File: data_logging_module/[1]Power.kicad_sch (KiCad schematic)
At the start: 14 parts, among them J3 Screw_Terminal_01x02, U2 TLV62569DBV

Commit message: Initial scheme
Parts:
- removed D9: D, Diode_SMD:D_PowerDI-123, symbol Device:D
- removed J3: Screw_Terminal_01x02, esp32s3_watches:terminal_block, symbol Connector:Screw_Terminal_01x02
- added C104, C105: 22u, Capacitor_SMD:C_0805_2012Metric, symbol Device:C
- added R107: 10R, Resistor_SMD:R_0805_2012Metric, symbol Device:R
- added U101: HT7533-1, Package_TO_SOT_SMD:SOT-89-3, symbol Regulator_Linear:HT75xx-1-SOT89
- renumbered C6 to C100, C7 to C101, C8 to C102, C9 to C103, C10 to C106, D10 to D100, L1 to L100, L2 to L101, R7 to R104, R8 to R105, R9 to R106, U2 to U100
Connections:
- net +5V: now also R107.2
- net GND: now also C104.2, C105.2, U101.1 (GND)
- new net +3.3VA: C105.1, U101.3 (VOUT)
- new net +5V_FILT: C104.1, R107.1, U101.2 (VIN)
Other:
- note added: "100mA max."
- note added: "Analog Supplies"
- note added: "C(in/out)>10uF"
- note added: "P(R)>1/8W"
- moved on the sheet: C100, C101, C102, C103, C106, D100, L100, L101, R104, R105, R106, U100

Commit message: BOM updates
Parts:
- C100, C101: Manufacturer Part Number (none) -> CL21B105KBFNNNE
- C102, C103: Manufacturer Part Number (none) -> CL21A226MAYNNNE
- C104, C105: value 22u -> 22uF; Manufacturer Samwha Capacitor -> Samsung Electro-Mechanics; Manufacturer Part Number CS2012X5R226M160NRE -> CL21A226MAYNNNE
- L100: Manufacturer Part Number (none) -> LQG18HN10NJ00D
- L101: footprint esp32s3_watches:MWSA0603S -> data_logging_module:MWSA0603S; Manufacturer Part Number (none) -> FXL0630-150-M
- R104: Manufacturer Part Number (none) -> 0805W8F1003T5E
- R105: Manufacturer Part Number (none) -> 0805W8F2202T5E
- R106: Manufacturer Part Number (none) -> ARG05FTC5000
- U100: Manufacturer Part Number (none) -> TLV62569DBVR
- U101: Manufacturer Part Number HT7533-1 -> HT7533-1
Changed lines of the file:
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@@
 			)
 		)
-		(property "Value" "22u"
+		(property "Value" "22uF"
 			(at 127 118.11 0)
 			(effects
@@
 			)
 		)
-		(property "Manufacturer" "Samwha Capacitor"
+		(property "Manufacturer" "Samsung Electro-Mechanics"
 			(at 123.19 116.84 0)
 			(effects
@@
 			)
 		)
-		(property "Manufacturer Part Number" "CS2012X5R226M160NRE"
+		(property "Manufacturer Part Number" "CL21A226MAYNNNE"
 			(at 123.19 116.84 0)
 			(effects
@@
 			)
 		)
+		(property "Manufacturer Part Number" "LQG18HN10NJ00D"
+			(at 77.47 45.72 0)
+			(effects
+				(font
+					(size 1.27 1.27)
+				)
+				(hide yes)
+			)
+		)
 		(pin "1"
 		)
@@
 			)
 		)
+		(property "Manufacturer Part Number" "CL21B105KBFNNNE"
+			(at 64.77 52.07 0)
+			(effects
+				(font
+					(size 1.27 1.27)
+				)
+				(hide yes)
+			)
+		)
 		(pin "1"
 		)
@@
 			)
 		)
+		(property "Manufacturer Part Number" "ARG05FTC5000"
+			(at 219.71 55.88 0)
+			(effects
+				(font
+					(size 1.27 1.27)
+				)
+				(hide yes)
+			)
+		)
 		(pin "1"
 		)
@@
 			)
 		)
-		(property "Manufacturer Part Number" "HT7533-1 "
+		(property "Manufacturer Part Number" "HT7533-1"
 			(at 106.68 113.03 0)
 			(effects
@@
 			)
 		)
+		(property "Manufacturer Part Number" "TLV62569DBVR"
+			(at 130.81 48.26 0)
+			(effects
+				(font
+					(size 1.27 1.27)
+				)
+				(hide yes)
+			)
+		)
 		(pin "1"
 		)
@@
 			)
 		)
+		(property "Manufacturer Part Number" "CL21A226MAYNNNE"
+			(at 163.83 52.07 0)
+			(effects
+				(font
+					(size 1.27 1.27)
+				)
+				(hide yes)
+			)
+		)
 		(pin "1"
 		)
@@
 		)
 		(property "Manufacturer Product Number" "CL21A226MAYNNNE"
+			(at 105.41 52.07 0)
+			(effects
+				(font
+					(size 1.27 1.27)
+				)
+				(hide yes)
+			)
+		)
+		(property "Manufacturer Part Number" "CL21A226MAYNNNE"
 			(at 105.41 52.07 0)
 			(effects
@@
 			)
 		)
-		(property "Value" "22u"
+		(property "Value" "22uF"
 			(at 93.98 118.11 0)
 			(effects
@@
 			)
 		)
-		(property "Manufacturer" "Samwha Capacitor"
+		(property "Manufacturer" "Samsung Electro-Mechanics"
 			(at 90.17 116.84 0)
 			(effects
@@
 			)
 		)
-		(property "Manufacturer Part Number" "CS2012X5R226M160NRE"
+		(property "Manufacturer Part Number" "CL21A226MAYNNNE"
 			(at 90.17 116.84 0)
 			(effects
@@
 			)
 		)
+		(property "Manufacturer Part Number" "CL21B105KBFNNNE"
+			(at 90.17 52.07 0)
+			(effects
+				(font
+					(size 1.27 1.27)
+				)
+				(hide yes)
+			)
+		)
 		(pin "1"
 		)
@@
 			)
 		)
-		(property "Footprint" "esp32s3_watches:MWSA0603S"
+		(property "Footprint" "data_logging_module:MWSA0603S"
 			(at 152.4 45.72 0)
 			(effects
@@
 		)
 		(property "Manufacturer Product Number" "FXL0630-150-M"
+			(at 152.4 45.72 0)
+			(effects
+				(font
+					(size 1.27 1.27)
+				)
+				(hide yes)
+			)
+		)
+		(property "Manufacturer Part Number" "FXL0630-150-M"
 			(at 152.4 45.72 0)
 			(effects
@@
 			)
 		)
+		(property "Manufacturer Part Number" "0805W8F1003T5E"
+			(at 181.61 52.07 0)
+			(effects
+				(font
+					(size 1.27 1.27)
+				)
+				(hide yes)
+			)
+		)
 		(pin "1"
 		)
@@
 			(at 181.61 66.04 0)
 			(effects
+				(font
+					(size 1.27 1.27)
+				)
+				(hide yes)
+			)
+		)
+		(property "Manufacturer Part Number" "0805W8F2202T5E"
+			(at 181.61 66.04 0)
+			(effects

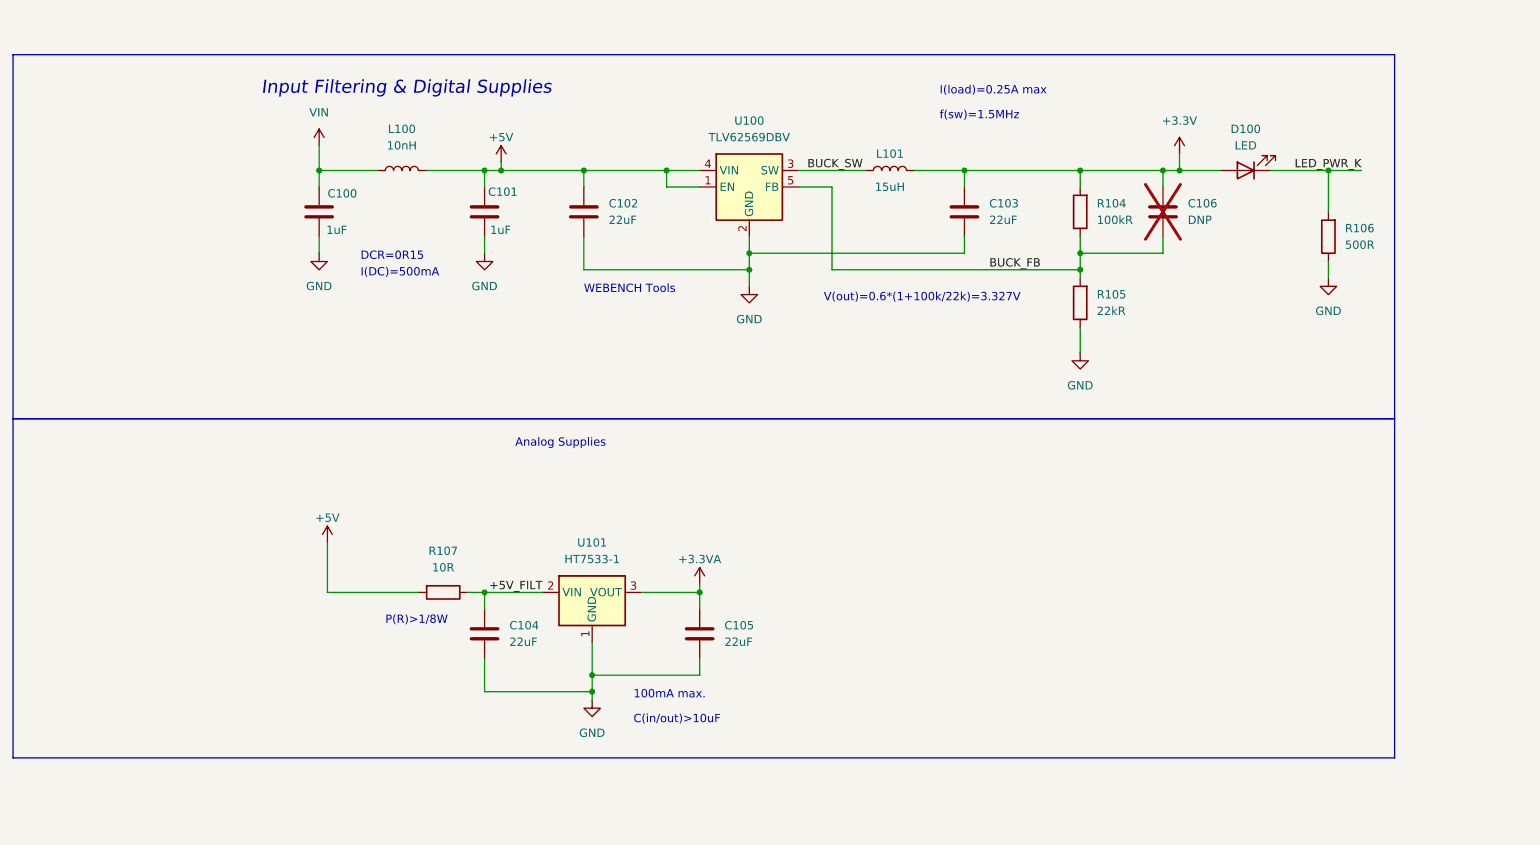
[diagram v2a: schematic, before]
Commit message: PCB initial layout
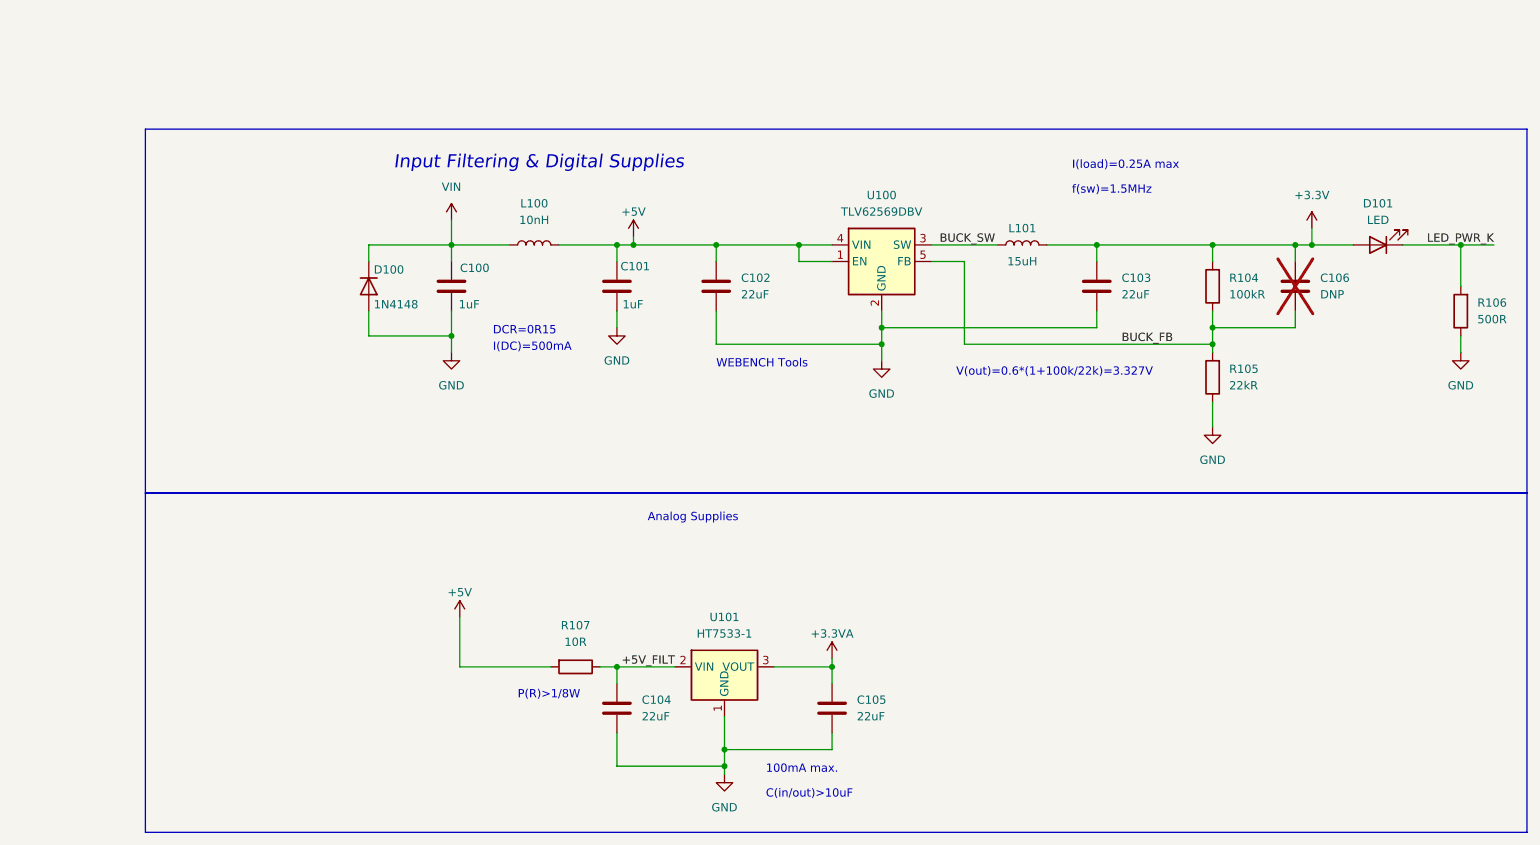
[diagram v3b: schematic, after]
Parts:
- added D100: 1N4148, Diode_SMD:D_SOD-123, symbol Device:D
- renumbered D100 to D101
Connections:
- net GND: now also D100.2 (A)
- net VIN: now also D100.1 (K)
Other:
- moved on the sheet: C100, C101, C102, C103, C104, C105, C106, D101, L100, L101, R104, R105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
